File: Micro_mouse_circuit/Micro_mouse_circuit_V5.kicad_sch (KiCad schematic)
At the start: 49 parts, among them J1 Conn_02x16_Odd_Even, J2 USB_C_Receptacle_PowerOnly_6P, J3 Conn_01x02, U1 HUSB237-AA001-DN06R, U10 AMS1117-3.3, U11 TPS22917DBV, U12 TPS22917DBV, U2 SK22D15L5, U3 LM2596SX-5_0/NOPB, U4 TP4056_C382139, U5 SN74LVC1G3157DCKR, U6 INA219AxDCN, U7 MT3608, U8 L298N_C19922, U9 L298N_C19922

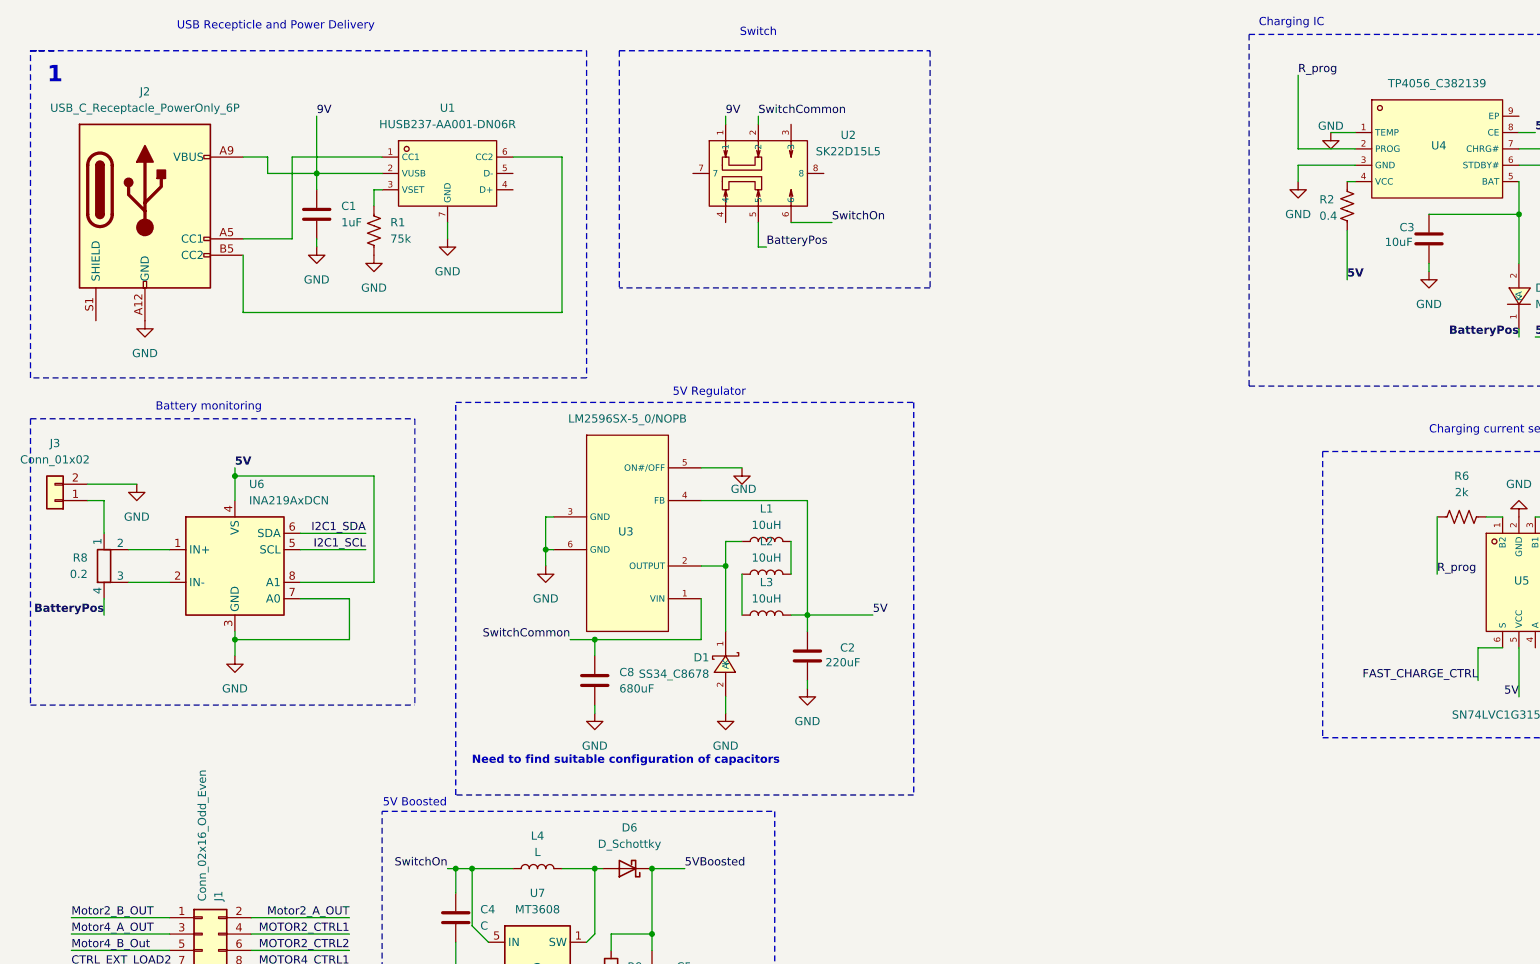
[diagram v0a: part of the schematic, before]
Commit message: Board System 5
-Includes block desegnations
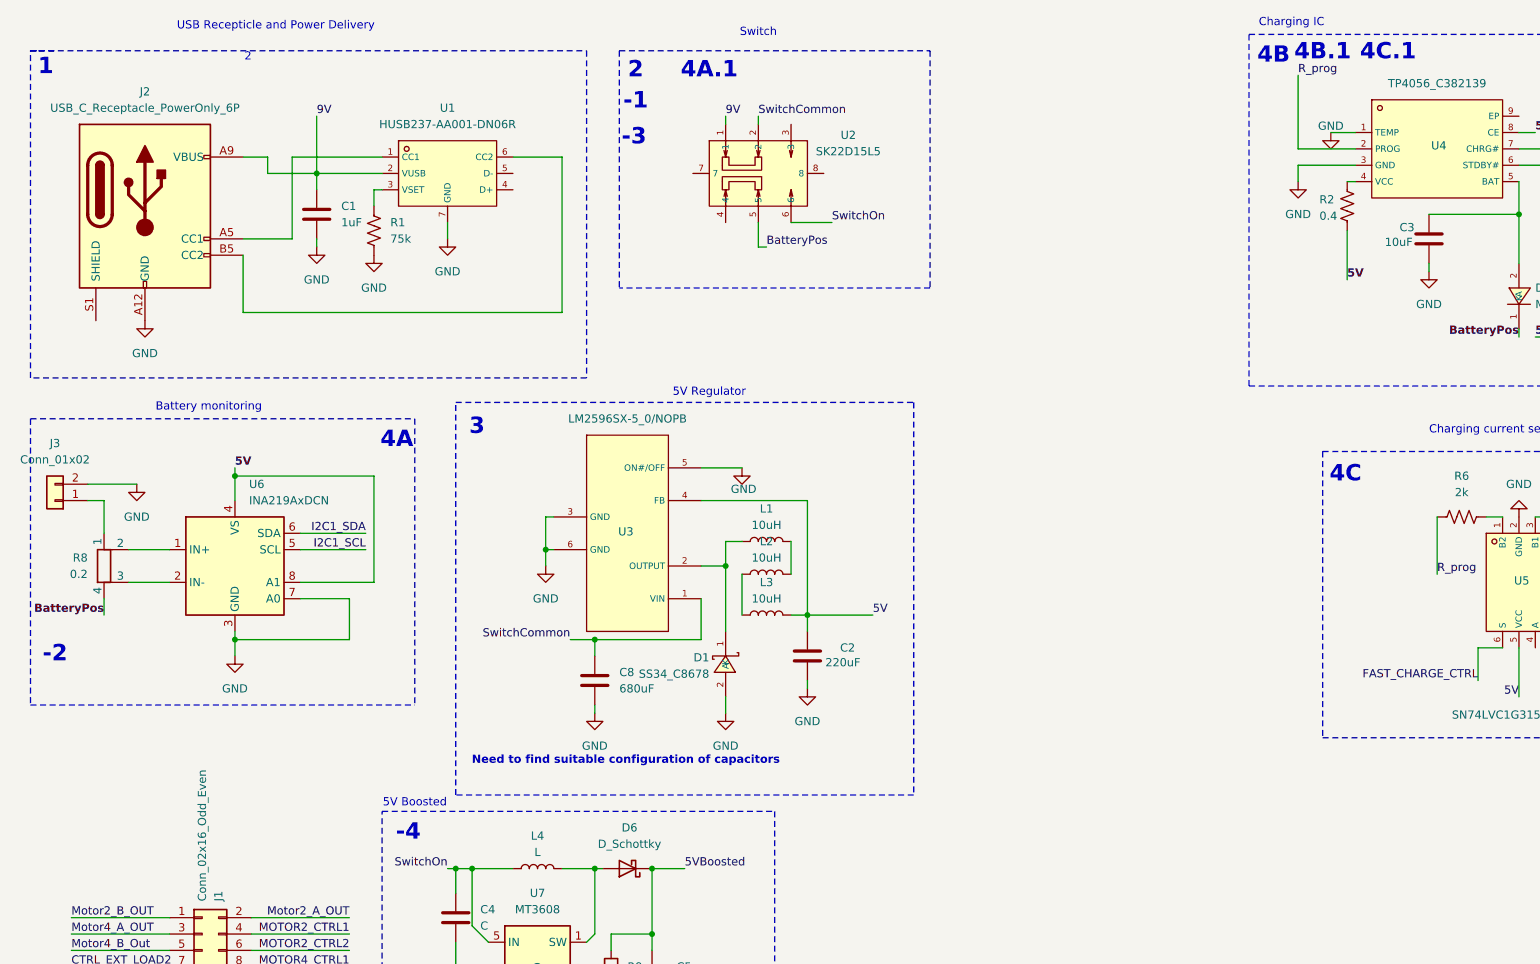
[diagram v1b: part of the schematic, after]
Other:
- note added: "-1"
- note added: "-2"
- note added: "-3"
- note added: "-4"
- note added: "2"
- note added: "3"
- note added: "4A"
- note added: "4A.1"
- note added: "4B"
- note added: "4B.1"
- note added: "4C"
- note added: "4C.1"
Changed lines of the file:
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@@
+		)
+	)
+	(text "2"
+		(exclude_from_sim no)
+		(at 109.22 23.368 0)
+		(effects
+			(font
+				(size 2.54 2.54)
+				(thickness 0.508)
+				(bold yes)
+			)
 		)
 	)
@@
 		)
 	)
+	(text "4B.1"
+		(exclude_from_sim no)
+		(at 215.9 20.574 0)
+		(effects
+			(font
+				(size 2.54 2.54)
+				(thickness 0.508)
+				(bold yes)
+			)
+		)
+	)
+	(text "4C"
+		(exclude_from_sim no)
+		(at 219.456 86.106 0)
+		(effects
+			(font
+				(size 2.54 2.54)
+				(thickness 0.508)
+				(bold yes)
+			)
+		)
+	)
 	(text "Charging IC\n"
 		(exclude_from_sim no)
@@
 		)
 	)
+	(text "4A.1"
+		(exclude_from_sim no)
+		(at 120.65 23.368 0)
+		(effects
+			(font
+				(size 2.54 2.54)
+				(thickness 0.508)
+				(bold yes)
+			)
+		)
+	)
 	(text "5V Regulator"
 		(exclude_from_sim no)
@@
 		)
 	)
+	(text "4B"
+		(exclude_from_sim no)
+		(at 208.28 21.082 0)
+		(effects
+			(font
+				(size 2.54 2.54)
+				(thickness 0.508)
+				(bold yes)
+			)
+		)
+	)
+	(text "-3"
+		(exclude_from_sim no)
+		(at 108.966 33.782 0)
+		(effects
+			(font
+				(size 2.54 2.54)
+				(thickness 0.508)
+				(bold yes)
+				(color 255 0 17 1)
+			)
+		)
+	)
 	(text "Charging current selector"
 		(exclude_from_sim no)
@@
 		)
 	)
+	(text "-4\n"
+		(exclude_from_sim no)
+		(at 73.914 141.732 0)
+		(effects
+			(font
+				(size 2.54 2.54)
+				(thickness 0.508)
+				(bold yes)
+				(color 255 0 17 1)
+			)
+		)
+	)
 	(text "5V Boosted"
 		(exclude_from_sim no)
@@
 		)
 	)
+	(text "-1"
+		(exclude_from_sim no)
+		(at 109.22 28.194 0)
+		(effects
+			(font
+				(size 2.54 2.54)
+				(thickness 0.508)
+				(bold yes)
+				(color 255 0 17 1)
+			)
+		)
+	)
+	(text "4A"
+		(exclude_from_sim no)
+		(at 72.136 80.772 0)
+		(effects
+			(font
+				(size 2.54 2.54)
+				(thickness 0.508)
+				(bold yes)
+			)
+		)
+	)
 	(text "Switch"
 		(exclude_from_sim no)
@@
 		)
 	)
+	(text "3"
+		(exclude_from_sim no)
+		(at 84.582 78.74 0)
+		(effects
+			(font
+				(size 2.54 2.54)
+				(thickness 0.508)
+				(bold yes)
+			)
+		)
+	)
 	(text "Need to find suitable configuration of capacitors"
 		(exclude_from_sim no)
@@
 	(text "1"
 		(exclude_from_sim no)
-		(at 19.05 24.13 0)
+		(at 17.6153 22.8654 0)
 		(effects
 			(font
@@
 		(effects
 			(font
+				(size 1.27 1.27)
+			)
+		)
+	)
+	(text "-2"
+		(exclude_from_sim no)
+		(at 19.05 114.046 0)
+		(effects
+			(font
+				(size 2.54 2.54)
+				(thickness 0.508)
+				(bold yes)
+				(color 255 0 17 1)
+			)
+		)
+	)
+	(text "4C.1"
+		(exclude_from_sim no)
+		(at 226.06 20.574 0)
+		(effects
+			(font
+				(size 2.54 2.54)
+				(thickness 0.508)
+				(bold yes)
+			)
+		)
+	)
+	(text "2"
+		(exclude_from_sim no)
+		(at 49.022 21.336 0)
+		(effects
+			(font

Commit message: 02/28 submission
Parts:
- removed C1: 1uF, symbol Device:C
- added C10: CL31B105KBHNNNE, xxcustom_footprint:C1206, symbol CL31B105KBHNNNE:CL31B105KBHNNNE
- added TP1, TP2, TP3: TestPoint, TestPoint:TestPoint_Pad_2.5x2.5mm, symbol Connector:TestPoint
- J2: footprint (none) -> xxcustom_footprint:USB-TYPE-C-SMD_TYPE-C-6P-LTH6.5
- R1: footprint (none) -> xxcustom_footprint:R0805
- R10: value R -> 10k
- R9: value R -> 45k
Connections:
- net 5VBoosted: now also TP1.1
- net 9V: now also C10.1
- net GND: now also R10.1, R6.1, R7.1, R9.2, U7.3 (FB), C10.2, TP2.1, TP3.1
- net R_prog: now also U5.4 (A); no longer R6.1, R7.1
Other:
- moved on the sheet: C5
